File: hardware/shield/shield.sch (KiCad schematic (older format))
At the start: 5 parts, among them J1 Conn_01x20, J2 Conn_01x20, U1 TMP36

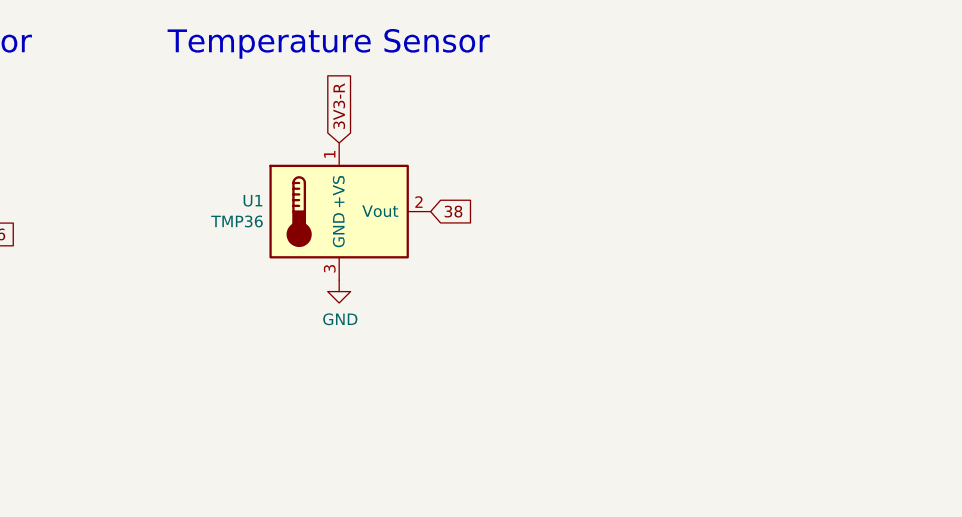
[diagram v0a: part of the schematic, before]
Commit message: updated shield for sparkfunESP32
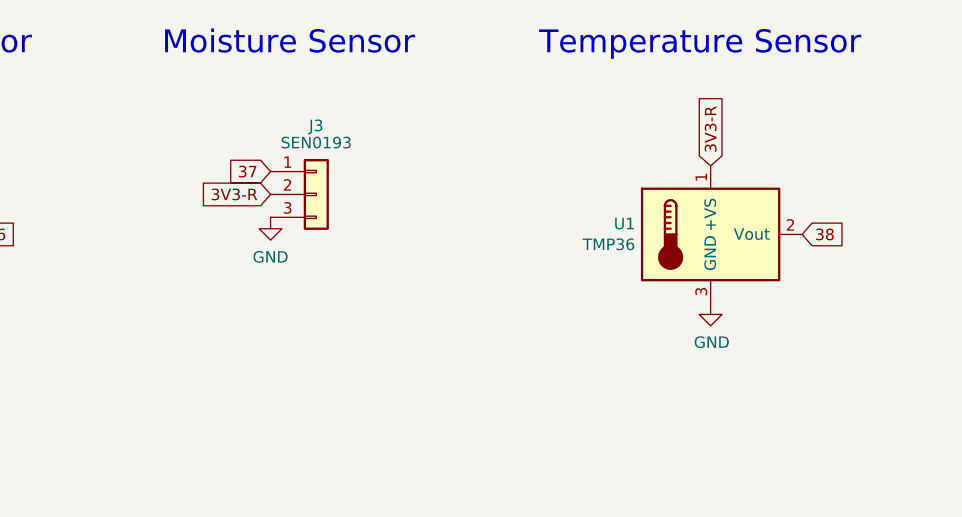
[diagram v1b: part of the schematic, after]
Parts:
- added J3: SEN0193, Connector_JST:JST_GH_SM03B-GHS-TB_1x03-1MP_P1.25mm_Horizontal, symbol Connector_Generic:Conn_01x03
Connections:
- net 37: now also J3.1 (Pin_1)
- net 3V3-R: now also J3.2 (Pin_2)
- net GND: now also J3.3 (Pin_3)
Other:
- note added: "Moisture Sensor"
- moved on the sheet: U1
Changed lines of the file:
@@
 L power:GND #PWR02
 U 1 1 5FAD2823
-P 2950 1800
-F 0 "#PWR02" H 2950 1550 50  0001 C CNN
-F 1 "GND" H 2955 1627 50  0000 C CNN
-F 2 "" H 2950 1800 50  0001 C CNN
-F 3 "" H 2950 1800 50  0001 C CNN
-	1    2950 1800
+P 4575 1900
+F 0 "#PWR02" H 4575 1650 50  0001 C CNN
+F 1 "GND" H 4580 1727 50  0000 C CNN
+F 2 "" H 4575 1900 50  0001 C CNN
+F 3 "" H 4575 1900 50  0001 C CNN
+	1    4575 1900
 	1    0    0    -1
 $EndComp
-Text GLabel 2950 1200 1    50   Input ~ 0
+Text GLabel 4575 1300 1    50   Input ~ 0
 3V3-R
-Text GLabel 3350 1500 2    50   Input ~ 0
+Text GLabel 4975 1600 2    50   Input ~ 0
 38
-Text Notes 2200 825  0    100  ~ 0
+Text Notes 3825 825  0    100  ~ 0
 Temperature Sensor
 $Comp
 L Sensor_Temperature:LM35-LP U1
 U 1 1 5FB449D9
-P 2950 1500
-F 0 "U1" H 2620 1546 50  0000 R CNN
-F 1 "TMP36" H 2620 1455 50  0000 R CNN
-F 2 "Package_TO_SOT_THT:TO-92L_Inline" H 3000 1250 50  0001 L CNN
-F 3 "http://www.ti.com/lit/ds/symlink/lm35.pdf" H 2950 1500 50  0001 C CNN
-	1    2950 1500
+P 4575 1600
+F 0 "U1" H 4245 1646 50  0000 R CNN
+F 1 "TMP36" H 4245 1555 50  0000 R CNN
+F 2 "Package_TO_SOT_THT:TO-92L_Inline" H 4625 1350 50  0001 L CNN
+F 3 "http://www.ti.com/lit/ds/symlink/lm35.pdf" H 4575 1600 50  0001 C CNN
+	1    4575 1600
 	1    0    0    -1
 $EndComp
+Text GLabel 2650 1425 0    50   Input ~ 0
+3V3-R
+$Comp
+L power:GND #PWR04
+U 1 1 5FB30986
+P 2650 1525
+F 0 "#PWR04" H 2650 1275 50  0001 C CNN
+F 1 "GND" H 2650 1350 50  0000 C CNN
+F 2 "" H 2650 1525 50  0001 C CNN
+F 3 "" H 2650 1525 50  0001 C CNN
+	1    2650 1525
+	1    0    0    -1
+$EndComp
+Text GLabel 2650 1325 0    50   Input ~ 0
+37
+Text Notes 2175 825  0    100  ~ 0
+Moisture Sensor
+$Comp
+L Connector_Generic:Conn_01x03 J3
+U 1 1 5FB2A1DF
+P 2850 1425
+F 0 "J3" H 2850 1725 50  0000 C CNN
+F 1 "SEN0193" H 2850 1650 50  0000 C CNN
+F 2 "Connector_JST:JST_GH_SM03B-GHS-TB_1x03-1MP_P1.25mm_Horizontal" H 2850 1425 50  0001 C CNN
+F 3 "~" H 2850 1425 50  0001 C CNN
+	1    2850 1425
+	1    0    0    -1
+$EndComp

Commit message: updated pcb connector, added logo and version number
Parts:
- J3: footprint Connector_JST:JST_GH_SM03B-GHS-TB_1x03-1MP_P1.25mm_Horizontal -> Connector_PinHeader_2.54mm:PinHeader_1x03_P2.54mm_Vertical
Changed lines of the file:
@@
 F 0 "J3" H 2850 1725 50  0000 C CNN
 F 1 "SEN0193" H 2850 1650 50  0000 C CNN
-F 2 "Connector_JST:JST_GH_SM03B-GHS-TB_1x03-1MP_P1.25mm_Horizontal" H 2850 1425 50  0001 C CNN
+F 2 "Connector_PinHeader_2.54mm:PinHeader_1x03_P2.54mm_Vertical" H 2850 1425 50  0001 C CNN
 F 3 "~" H 2850 1425 50  0001 C CNN
 	1    2850 1425

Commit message: Revert "Thomas object detection"
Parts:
- J3: footprint Connector_PinHeader_2.54mm:PinHeader_1x03_P2.54mm_Vertical -> Connector_JST:JST_GH_SM03B-GHS-TB_1x03-1MP_P1.25mm_Horizontal
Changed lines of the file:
@@
 F 0 "J3" H 2850 1725 50  0000 C CNN
 F 1 "SEN0193" H 2850 1650 50  0000 C CNN
-F 2 "Connector_PinHeader_2.54mm:PinHeader_1x03_P2.54mm_Vertical" H 2850 1425 50  0001 C CNN
+F 2 "Connector_JST:JST_GH_SM03B-GHS-TB_1x03-1MP_P1.25mm_Horizontal" H 2850 1425 50  0001 C CNN
 F 3 "~" H 2850 1425 50  0001 C CNN
 	1    2850 1425
